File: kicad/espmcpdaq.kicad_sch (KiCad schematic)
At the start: 28 parts, among them J1 Conn_01x02, J2 Conn_01x15_Female, J3 Conn_01x15_Female

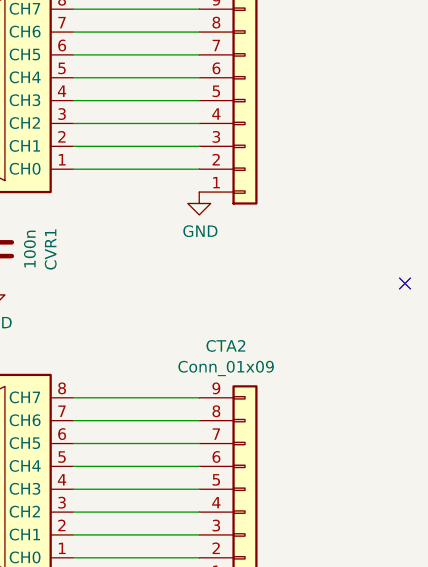
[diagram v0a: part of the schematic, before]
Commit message: Corrected hte ERC problems.
The issues kind of make sense. Since the same MISO and MOSI are used for every ADC, the system complains about connecting different outputs together. This not an issue because each ADC has different chip select wire. There were several warnings about unspecified pins connected to some other pins. I just asked KiCAD to ignore this

I still need to think about power supply for the board. The anemometers will use 24V and I could reduce this to 5V using a 78-5 or LM317 but they will run hot due to the large voltage drop. Another thing I should think about is how adding a button to select voltage source: USB or power supply. I think I will rearrange everything and add this feature.
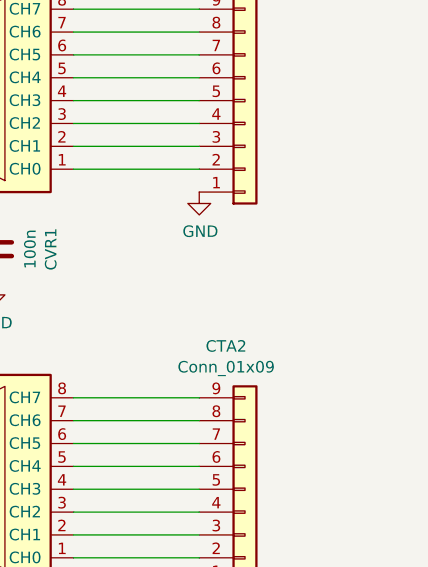
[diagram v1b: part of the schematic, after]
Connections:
- no-connect marks 22 -> 21
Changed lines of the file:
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@@
-	)
-	(no_connect
-		(at 271.78 83.82)
 	)
 	(no_connect
@@
 	(label "Vref"
 		(at 222.25 119.38 270)
+		(fields_autoplaced yes)
 		(effects
 			(font
@@
 	(label "MISO"
 		(at 154.94 146.05 180)
+		(fields_autoplaced yes)
 		(effects
 			(font
@@
 	(label "VDD"
 		(at 74.93 73.66 90)
+		(fields_autoplaced yes)
 		(effects
 			(font
@@
 	(label "CS2"
 		(at 204.47 101.6 180)
+		(fields_autoplaced yes)
 		(effects
 			(font
@@
 	(label "MOSI"
 		(at 92.71 143.51 180)
+		(fields_autoplaced yes)
 		(effects
 			(font
@@
 	(label "CLK"
 		(at 154.94 148.59 180)
+		(fields_autoplaced yes)
 		(effects
 			(font
@@
 	(label "MISO"
 		(at 64.77 144.78 0)
+		(fields_autoplaced yes)
 		(effects
 			(font
@@
 	(label "MISO"
 		(at 204.47 106.68 180)
+		(fields_autoplaced yes)
 		(effects
 			(font
@@
 	(label "CLK"
 		(at 204.47 66.04 180)
+		(fields_autoplaced yes)
 		(effects
 			(font
@@
 	(label "CLK"
 		(at 204.47 109.22 180)
+		(fields_autoplaced yes)
 		(effects
 			(font
@@
 	(label "CS4"
 		(at 92.71 140.97 180)
+		(fields_autoplaced yes)
 		(effects
 			(font
@@
 	(label "CS1"
 		(at 204.47 58.42 180)
+		(fields_autoplaced yes)
 		(effects
 			(font
@@
 	(label "CS3"
 		(at 154.94 140.97 180)
+		(fields_autoplaced yes)
 		(effects
 			(font
@@
 	(label "VDD"
 		(at 214.63 119.38 270)
+		(fields_autoplaced yes)
 		(effects
 			(font
@@
 	(label "MOSI"
 		(at 154.94 143.51 180)
+		(fields_autoplaced yes)
 		(effects
 			(font
@@
 	(label "Vref"
 		(at 110.49 81.28 180)
+		(fields_autoplaced yes)
 		(effects
 			(font
@@
 	(label "MOSI"
 		(at 64.77 132.08 0)
+		(fields_autoplaced yes)
 		(effects
 			(font
@@
 	(label "CS1"
 		(at 64.77 149.86 0)
+		(fields_autoplaced yes)
 		(effects
 			(font
@@
 	(label "MOSI"
 		(at 204.47 104.14 180)
+		(fields_autoplaced yes)
 		(effects
 			(font
@@
 	(label "VDD"
 		(at 110.49 76.2 90)
+		(fields_autoplaced yes)
 		(effects
 			(font
@@
 	(label "VDD"
 		(at 165.1 158.75 270)
+		(fields_autoplaced yes)
 		(effects
 			(font
@@
 	(label "Vref"
 		(at 110.49 158.75 270)
+		(fields_autoplaced yes)
 		(effects
 			(font
@@
 	(label "Vref"
 		(at 185.42 24.13 270)
+		(fields_autoplaced yes)
 		(effects
 			(font
@@
 	(label "Vref"
 		(at 77.47 82.55 0)
+		(fields_autoplaced yes)
 		(effects
 			(font
@@
 	(label "VDD"
 		(at 102.87 158.75 270)
+		(fields_autoplaced yes)
 		(effects
 			(font
@@
 	(label "CS4"
 		(at 48.26 152.4 180)
+		(fields_autoplaced yes)
 		(effects
 			(font
@@
 	(label "Vref"
 		(at 172.72 158.75 270)
+		(fields_autoplaced yes)
 		(effects
 			(font
@@
 	(label "VDD"
 		(at 196.85 24.13 270)
+		(fields_autoplaced yes)
 		(effects
 			(font
@@
 	(label "VDD"
 		(at 214.63 76.2 270)
+		(fields_autoplaced yes)
 		(effects
 			(font
@@
 	(label "MOSI"
 		(at 204.47 60.96 180)
+		(fields_autoplaced yes)
 		(effects
 			(font
@@
 	(label "CS2"
 		(at 64.77 134.62 0)
+		(fields_autoplaced yes)
 		(effects
 			(font
@@
 	(label "VDD"
 		(at 48.26 167.64 180)
+		(fields_autoplaced yes)
 		(effects
 			(font
@@
 	(label "Vref"
 		(at 222.25 76.2 270)
+		(fields_autoplaced yes)
 		(effects
 			(font
@@
 	(label "MISO"
 		(at 92.71 146.05 180)
+		(fields_autoplaced yes)
 		(effects
 			(font
@@
 	(label "CLK"
 		(at 64.77 147.32 0)
+		(fields_autoplaced yes)
 		(effects
 			(font
@@
 	(label "MISO"
 		(at 204.47 63.5 180)
+		(fields_autoplaced yes)
 		(effects
 			(font
@@
 	(label "CS3"
 		(at 48.26 149.86 180)
+		(fields_autoplaced yes)
 		(effects
 			(font
@@
 	(label "CLK"
 		(at 92.71 148.59 180)
-		(effects
-			(font
+		(fields_autoplaced yes)
+		(effects
+			(font

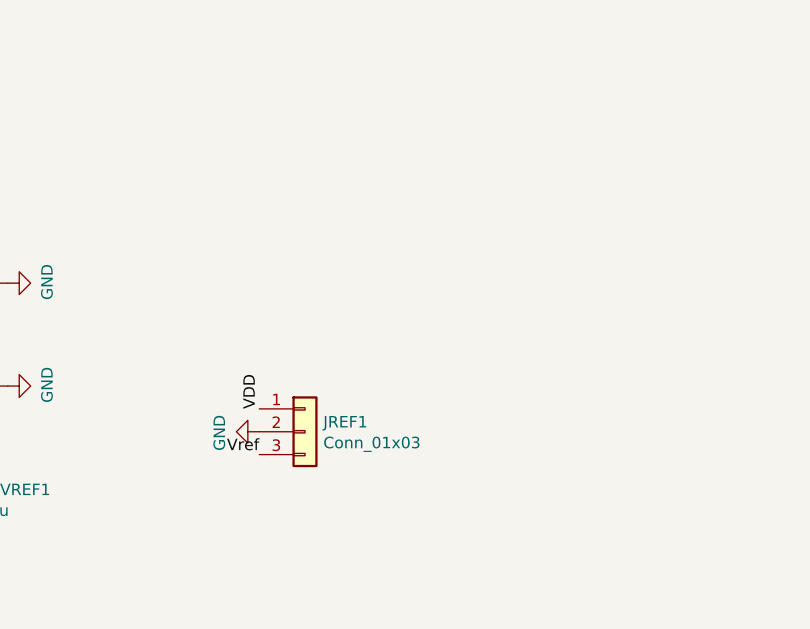
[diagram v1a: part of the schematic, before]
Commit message: Added the possibility of choosing 5V input.
The 5V input can come from either a terminal or the esp board USB.

I've been thinking and I believe I should make the daq part independent
of the board. Therefore I should deal only with SPI lines and input voltage.
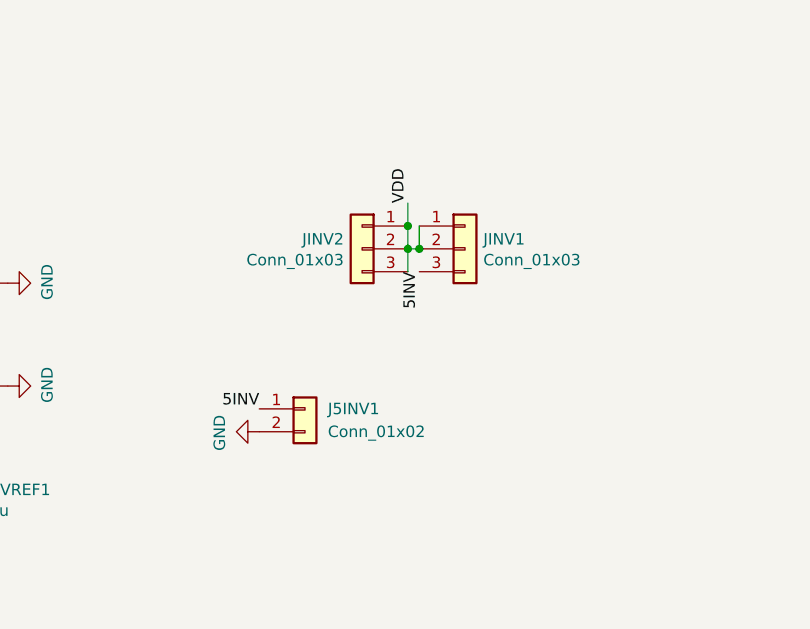
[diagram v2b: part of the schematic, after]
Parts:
- removed JREF1: Conn_01x03, TerminalBlock:TerminalBlock_bornier-3_P5.08mm, symbol Connector_Generic:Conn_01x03
- added J5INV1: Conn_01x02, TerminalBlock:TerminalBlock_bornier-2_P5.08mm, symbol Connector_Generic:Conn_01x02
- added JINV1, JINV2: Conn_01x03, Connector_PinHeader_2.54mm:PinHeader_1x03_P2.54mm_Vertical, symbol Connector_Generic:Conn_01x03
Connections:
- net GND: now also J5INV1.2 (Pin_2)
- net VDD: now also JINV1.1 (Pin_1), JINV1.2 (Pin_2), JINV2.1 (Pin_1), JINV2.2 (Pin_2), JINV2.3 (Pin_3)
- new net 5INV: J5INV1.1 (Pin_1), JINV1.3 (Pin_3)
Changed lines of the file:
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@@
 	(paper "A4")
 	(junction
+		(at 127 58.42)
+		(diameter 0)
+		(color 0 0 0 0)
+	)
+	(junction
 		(at 74.93 81.28)
 		(diameter 0)
@@
 	)
 	(junction
+		(at 127 55.88)
+		(diameter 0)
+		(color 0 0 0 0)
+	)
+	(junction
 		(at 69.85 82.55)
 		(diameter 0)
@@
 	)
 	(junction
+		(at 128.27 58.42)
+		(diameter 0)
+		(color 0 0 0 0)
+	)
+	(junction
 		(at 74.93 73.66)
 		(diameter 0)
@@
 	(wire
 		(pts
+			(xy 127 55.88) (xy 127 58.42)
+		)
+		(stroke
+			(width 0)
+			(type default)
+		)
+	)
+	(wire
+		(pts
 			(xy 234.95 111.76) (xy 248.92 111.76)
 		)
@@
 	(wire
 		(pts
+			(xy 128.27 55.88) (xy 128.27 58.42)
+		)
+		(stroke
+			(width 0)
+			(type default)
+		)
+	)
+	(wire
+		(pts
 			(xy 72.39 69.85) (xy 72.39 81.28)
 		)
@@
 	(wire
 		(pts
+			(xy 127 53.34) (xy 127 55.88)
+		)
+		(stroke
+			(width 0)
+			(type default)
+		)
+	)
+	(wire
+		(pts
 			(xy 72.39 81.28) (xy 74.93 81.28)
 		)
@@
 	(wire
 		(pts
+			(xy 127 58.42) (xy 128.27 58.42)
+		)
+		(stroke
+			(width 0)
+			(type default)
+		)
+	)
+	(wire
+		(pts
 			(xy 234.95 63.5) (xy 248.92 63.5)
 		)
@@
 	(wire
 		(pts
+			(xy 127 58.42) (xy 127 60.96)
+		)
+		(stroke
+			(width 0)
+			(type default)
+		)
+	)
+	(wire
+		(pts
 			(xy 69.85 81.28) (xy 72.39 81.28)
 		)
@@
 		)
 	)
-	(label "Vref"
-		(at 110.49 81.28 180)
+	(label "5INV"
+		(at 110.49 76.2 180)
 		(fields_autoplaced yes)
 		(effects
@@
 	)
 	(label "VDD"
-		(at 110.49 76.2 90)
+		(at 127 53.34 90)
 		(fields_autoplaced yes)
 		(effects
@@
 		)
 	)
+	(label "5INV"
+		(at 128.27 60.96 270)
+		(fields_autoplaced yes)
+		(effects
+			(font
+				(size 1.27 1.27)
+			)
+			(justify right bottom)
+		)
+	)
 	(label "VDD"
 		(at 48.26 167.64 180)
@@
 	)
 	(symbol
-		(lib_id "Connector_Generic:Conn_01x03")
-		(at 115.57 78.74 0)
-		(unit 1)
-		(exclude_from_sim no)
-		(in_bom yes)
-		(on_board yes)
-		(dnp no)
-		(property "Reference" "JREF1"
-			(at 117.602 77.6732 0)
-			(effects
-				(font
-					(size 1.27 1.27)
-				)
-				(justify left)
-			)
-		)
-		(property "Value" "Conn_01x03"
-			(at 117.602 79.9846 0)
-			(effects
-				(font
-					(size 1.27 1.27)
-				)
-				(justify left)
-			)
-		)
-		(property "Footprint" "TerminalBlock:TerminalBlock_bornier-3_P5.08mm"
-			(at 115.57 78.74 0)
-			(effects
-				(font
-					(size 1.27 1.27)
-				)
-				(hide yes)
-			)
-		)
-		(property "Datasheet" "~"
-			(at 115.57 78.74 0)
-			(effects
-				(font
-					(size 1.27 1.27)
-				)
-				(hide yes)
-			)
-		)
-		(property "Description" ""
-			(at 115.57 78.74 0)
-			(effects
-				(font
-					(size 1.27 1.27)
-				)
-				(hide yes)
-			)
-		)
-		(pin "1"
-		)
-		(pin "2"
-		)
-		(pin "3"
-		)
-		(instances
-			(project ""
-				(path "/a9e92cc9-9cb0-45d3-aac2-4432c6b1bd92"
-					(reference "JREF1")
-					(unit 1)
-				)
-			)
-		)
-	)
-	(symbol
 		(lib_id "espmcpdaq-rescue:GND-power")
 		(at 110.49 78.74 270)
@@
 					(unit 1)
 				)
+			)
+		)
+	)
+	(symbol
+		(lib_id "Connector_Generic:Conn_01x03")
+		(at 121.92 58.42 0)
+		(mirror y)
+		(unit 1)
+		(exclude_from_sim no)
+		(in_bom yes)
+		(on_board yes)
+		(dnp no)
+		(property "Reference" "JINV2"
+			(at 119.888 57.3532 0)
+			(effects
+				(font
+					(size 1.27 1.27)
+				)
+				(justify left)
+			)
+		)
+		(property "Value" "Conn_01x03"
+			(at 119.888 59.6646 0)
+			(effects
+				(font
+					(size 1.27 1.27)
+				)
+				(justify left)
+			)
+		)
+		(property "Footprint" "Connector_PinHeader_2.54mm:PinHeader_1x03_P2.54mm_Vertical"
+			(at 121.92 58.42 0)
+			(effects
+				(font
+					(size 1.27 1.27)
+				)
+				(hide yes)
+			)
+		)
+		(property "Datasheet" "~"
+			(at 121.92 58.42 0)
+			(effects
+				(font
+					(size 1.27 1.27)
+				)
+				(hide yes)
+			)
+		)
+		(property "Description" ""
+			(at 121.92 58.42 0)
+			(effects
+				(font
+					(size 1.27 1.27)
+				)
+				(hide yes)
+			)
+		)
+		(pin "1"
+		)
+		(pin "2"
+		)
+		(pin "3"
+		)
+		(instances
+			(project "espmcpdaq"
+				(path "/a9e92cc9-9cb0-45d3-aac2-4432c6b1bd92"
+					(reference "JINV2")
+					(unit 1)
+				)
+			)
+		)
+	)
+	(symbol
+		(lib_id "Connector_Generic:Conn_01x02")
+		(at 115.57 76.2 0)
+		(unit 1)
+		(exclude_from_sim no)
+		(in_bom yes)
+		(on_board yes)
+		(dnp no)
+		(fields_autoplaced yes)
+		(property "Reference" "J5INV1"
+			(at 118.11 76.1999 0)
+			(effects
+				(font
+					(size 1.27 1.27)
+				)
+				(justify left)
+			)
+		)
+		(property "Value" "Conn_01x02"
+			(at 118.11 78.7399 0)
+			(effects
+				(font
+					(size 1.27 1.27)
+				)
+				(justify left)
+			)
+		)
+		(property "Footprint" "TerminalBlock:TerminalBlock_bornier-2_P5.08mm"
+			(at 115.57 76.2 0)
+			(effects
+				(font
+					(size 1.27 1.27)
+				)
+				(hide yes)
+			)
+		)
+		(property "Datasheet" "~"
+			(at 115.57 76.2 0)
+			(effects
+				(font
+					(size 1.27 1.27)
+				)
+				(hide yes)
+			)
+		)
+		(property "Description" "Generic connector, single row, 01x02, script generated (kicad-library-utils/schlib/autogen/connector/)"
+			(at 115.57 76.2 0)
+			(effects
+				(font
+					(size 1.27 1.27)
+				)
+				(hide yes)
+			)
+		)
+		(pin "2"
+		)
+		(pin "1"
+		)
+		(instances
+			(project ""
+				(path "/a9e92cc9-9cb0-45d3-aac2-4432c6b1bd92"
+					(reference "J5INV1")
+					(unit 1)
+				)
+			)
+		)
+	)
+	(symbol
+		(lib_id "Connector_Generic:Conn_01x03")
+		(at 133.35 58.42 0)
+		(unit 1)
+		(exclude_from_sim no)
+		(in_bom yes)
+		(on_board yes)
+		(dnp no)
+		(property "Reference" "JINV1"
+			(at 135.382 57.3532 0)
+			(effects
+				(font
+					(size 1.27 1.27)
+				)
+				(justify left)
+			)
+		)
+		(property "Value" "Conn_01x03"
+			(at 135.382 59.6646 0)
+			(effects
+				(font
+					(size 1.27 1.27)
+				)
+				(justify left)
+			)
+		)
+		(property "Footprint" "Connector_PinHeader_2.54mm:PinHeader_1x03_P2.54mm_Vertical"
+			(at 133.35 58.42 0)
+			(effects
+				(font
+					(size 1.27 1.27)
+				)
+				(hide yes)
+			)
+		)
+		(property "Datasheet" "~"
+			(at 133.35 58.42 0)
+			(effects
+				(font
+					(size 1.27 1.27)
+				)
+				(hide yes)
+			)
+		)
+		(property "Description" ""
+			(at 133.35 58.42 0)
+			(effects
+				(font
+					(size 1.27 1.27)
+				)
+				(hide yes)
+			)
+		)
+		(pin "1"
+		)
+		(pin "2"
+		)
+		(pin "3"
+		)
+		(instances
+			(project "espmcpdaq"
+				(path "/a9e92cc9-9cb0-45d3-aac2-4432c6b1bd92"
+					(reference "JINV1")
+					(unit 1)
+				)
